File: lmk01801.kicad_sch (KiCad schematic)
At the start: 41 parts, among them J1001 142-0701-201, J1002 U.FL-R-SMT(10), J1003 U.FL-R-SMT(10), J1004 142-0701-201, J1005 U.FL-R-SMT(10), T1001 TCM2-43X+, T1002 TCM2-43X+, U1001 TCP-2-33W+, U1002 LMK01801BISQE/NOPB

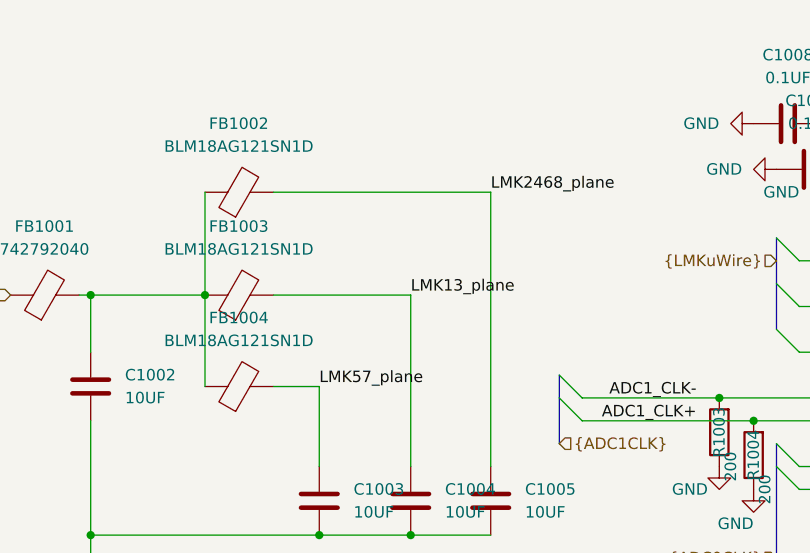
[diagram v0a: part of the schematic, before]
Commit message: Updates from Michal to fix ERC errors
Still lots of ERC warnings
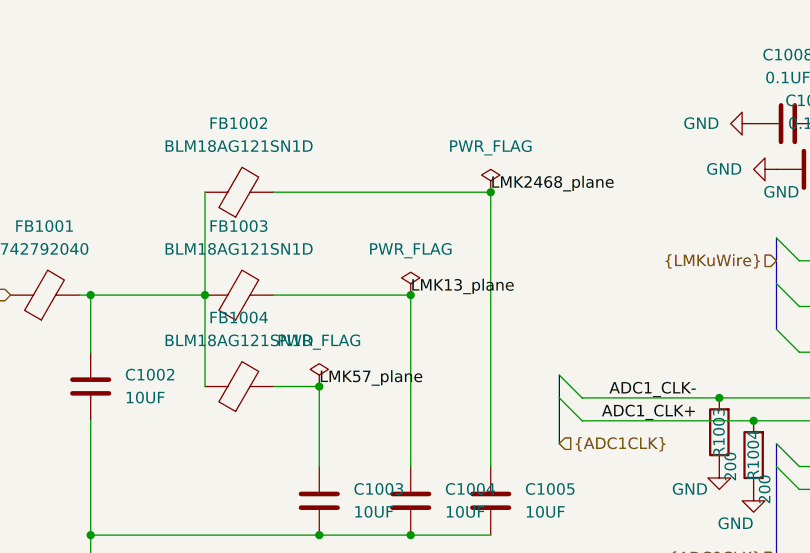
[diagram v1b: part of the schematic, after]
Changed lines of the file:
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@@
 	)
 	(junction
+		(at 64.77 54.61)
+		(diameter 0)
+		(color 0 0 0 0)
+	)
+	(junction
 		(at 123.19 114.3)
 		(diameter 0)
@@
 	)
 	(junction
+		(at 83.82 33.02)
+		(diameter 0)
+		(color 0 0 0 0)
+	)
+	(junction
 		(at 120.65 63.5)
 		(diameter 0)
@@
 		(color 0 0 0 0)
 	)
+	(junction
+		(at 74.93 44.45)
+		(diameter 0)
+		(color 0 0 0 0)
+	)
 	(no_connect
 		(at 245.11 106.68)
@@
 	(wire
 		(pts
+			(xy 120.65 25.4) (xy 143.51 25.4)
+		)
+		(stroke
+			(width 0)
+			(type default)
+		)
+	)
+	(wire
+		(pts
 			(xy 35.56 124.46) (xy 39.37 124.46)
 		)
@@
 	(wire
 		(pts
-			(xy 120.65 25.4) (xy 143.51 25.4)
-		)
-		(stroke
-			(width 0)
-			(type default)
-		)
-	)
-	(wire
-		(pts
 			(xy 245.11 33.02) (xy 266.7 33.02)
 		)
@@
 	)
 	(symbol
+		(lib_id "power:PWR_FLAG")
+		(at 64.77 54.61 0)
+		(unit 1)
+		(exclude_from_sim no)
+		(in_bom yes)
+		(on_board yes)
+		(dnp no)
+		(fields_autoplaced yes)
+		(property "Reference" "#FLG03"
+			(at 64.77 52.705 0)
+			(effects
+				(font
+					(size 1.27 1.27)
+				)
+				(hide yes)
+			)
+		)
+		(property "Value" "PWR_FLAG"
+			(at 64.77 49.53 0)
+			(effects
+				(font
+					(size 1.27 1.27)
+				)
+			)
+		)
+		(property "Footprint" ""
+			(at 64.77 54.61 0)
+			(effects
+				(font
+					(size 1.27 1.27)
+				)
+				(hide yes)
+			)
+		)
+		(property "Datasheet" "~"
+			(at 64.77 54.61 0)
+			(effects
+				(font
+					(size 1.27 1.27)
+				)
+				(hide yes)
+			)
+		)
+		(property "Description" "Special symbol for telling ERC where power comes from"
+			(at 64.77 54.61 0)
+			(effects
+				(font
+					(size 1.27 1.27)
+				)
+				(hide yes)
+			)
+		)
+		(pin "1"
+		)
+		(instances
+			(project "zest"
+				(path "/00000000-0000-0000-0000-000000000003/00000000-0000-0000-0000-000000000015"
+					(reference "#FLG03")
+					(unit 1)
+				)
+			)
+		)
+	)
+	(symbol
 		(lib_id "power:GND")
 		(at 214.63 157.48 0)
@@
 	)
 	(symbol
+		(lib_id "power:PWR_FLAG")
+		(at 83.82 33.02 0)
+		(unit 1)
+		(exclude_from_sim no)
+		(in_bom yes)
+		(on_board yes)
+		(dnp no)
+		(fields_autoplaced yes)
+		(property "Reference" "#FLG01"
+			(at 83.82 31.115 0)
+			(effects
+				(font
+					(size 1.27 1.27)
+				)
+				(hide yes)
+			)
+		)
+		(property "Value" "PWR_FLAG"
+			(at 83.82 27.94 0)
+			(effects
+				(font
+					(size 1.27 1.27)
+				)
+			)
+		)
+		(property "Footprint" ""
+			(at 83.82 33.02 0)
+			(effects
+				(font
+					(size 1.27 1.27)
+				)
+				(hide yes)
+			)
+		)
+		(property "Datasheet" "~"
+			(at 83.82 33.02 0)
+			(effects
+				(font
+					(size 1.27 1.27)
+				)
+				(hide yes)
+			)
+		)
+		(property "Description" "Special symbol for telling ERC where power comes from"
+			(at 83.82 33.02 0)
+			(effects
+				(font
+					(size 1.27 1.27)
+				)
+				(hide yes)
+			)
+		)
+		(pin "1"
+		)
+		(instances
+			(project "zest"
+				(path "/00000000-0000-0000-0000-000000000003/00000000-0000-0000-0000-000000000015"
+					(reference "#FLG01")
+					(unit 1)
+				)
+			)
+		)
+	)
+	(symbol
 		(lib_id "Device:C")
 		(at 264.16 25.4 90)
@@
 					(unit 1)
 				)
+			)
+		)
+	)
+	(symbol
+		(lib_id "power:PWR_FLAG")
+		(at 74.93 44.45 0)
+		(unit 1)
+		(exclude_from_sim no)
+		(in_bom yes)
+		(on_board yes)
+		(dnp no)
+		(fields_autoplaced yes)
+		(property "Reference" "#FLG02"
+			(at 74.93 42.545 0)
+			(effects
+				(font
+					(size 1.27 1.27)
+				)
+				(hide yes)
+			)
+		)
+		(property "Value" "PWR_FLAG"
+			(at 74.93 39.37 0)
+			(effects
+				(font
+					(size 1.27 1.27)
+				)
+			)
+		)
+		(property "Footprint" ""
+			(at 74.93 44.45 0)
+			(effects
+				(font
+					(size 1.27 1.27)
+				)
+				(hide yes)
+			)
+		)
+		(property "Datasheet" "~"
+			(at 74.93 44.45 0)
+			(effects
+				(font
+					(size 1.27 1.27)
+				)
+				(hide yes)
+			)
+		)
+		(property "Description" "Special symbol for telling ERC where power comes from"
+			(at 74.93 44.45 0)
+			(effects
+				(font
+					(size 1.27 1.27)
+				)
+				(hide yes)
+			)
+		)
+		(pin "1"
+		)
+		(instances
+			(project "zest"
+				(path "/00000000-0000-0000-0000-000000000003/00000000-0000-0000-0000-000000000015"
+					(reference "#FLG02")
+					(unit 1)
+				)

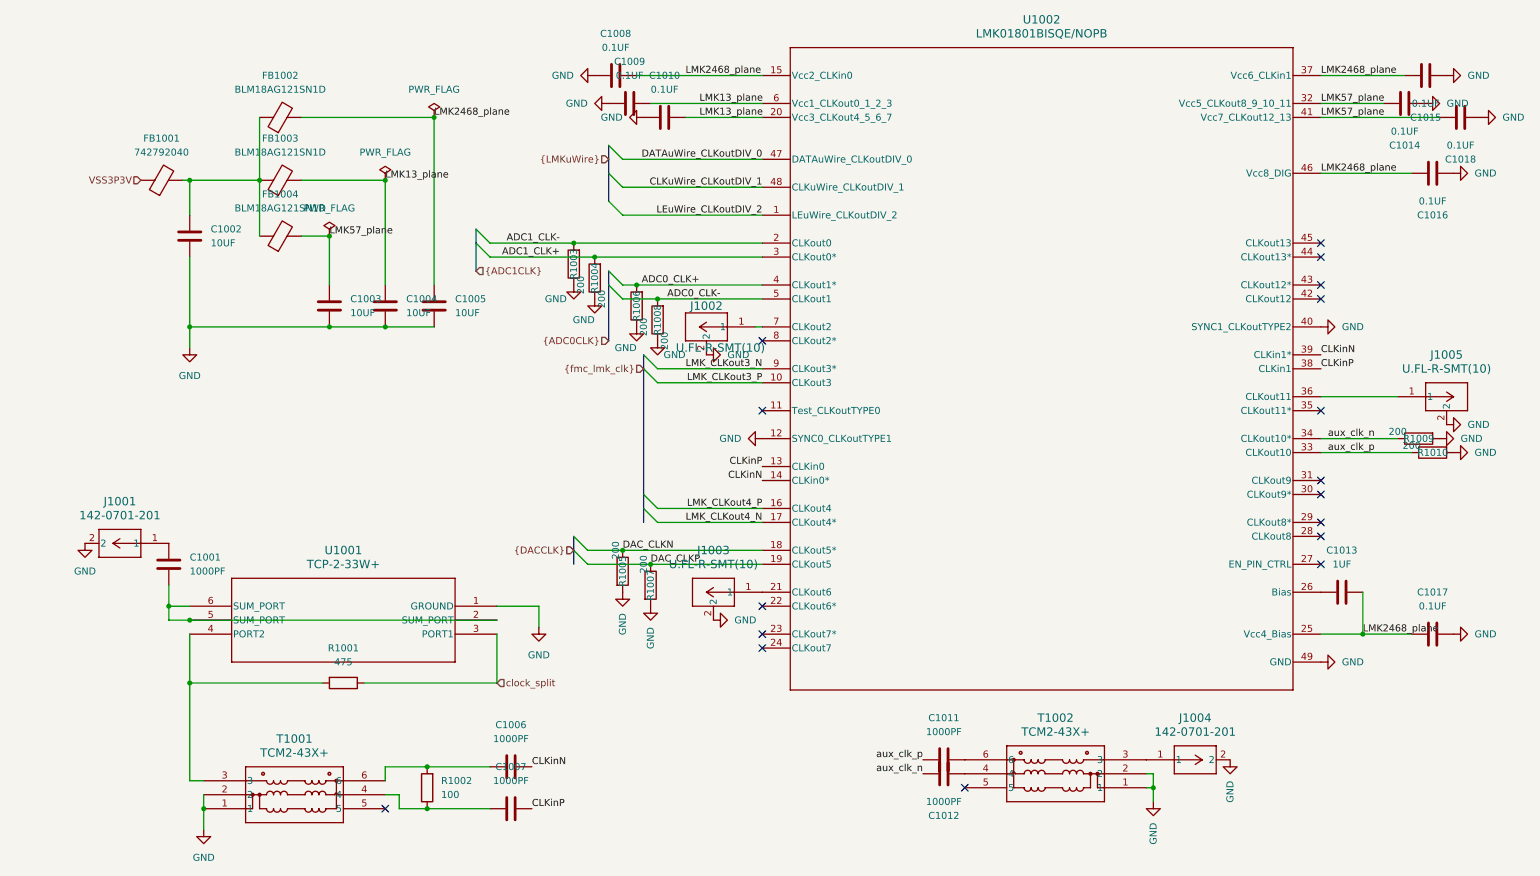
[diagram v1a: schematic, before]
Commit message: Schematic Changes
Added Manufacturer/MPN/Description Fields to parts
Added libraries to project
Modified FMC schematic to use new symbol
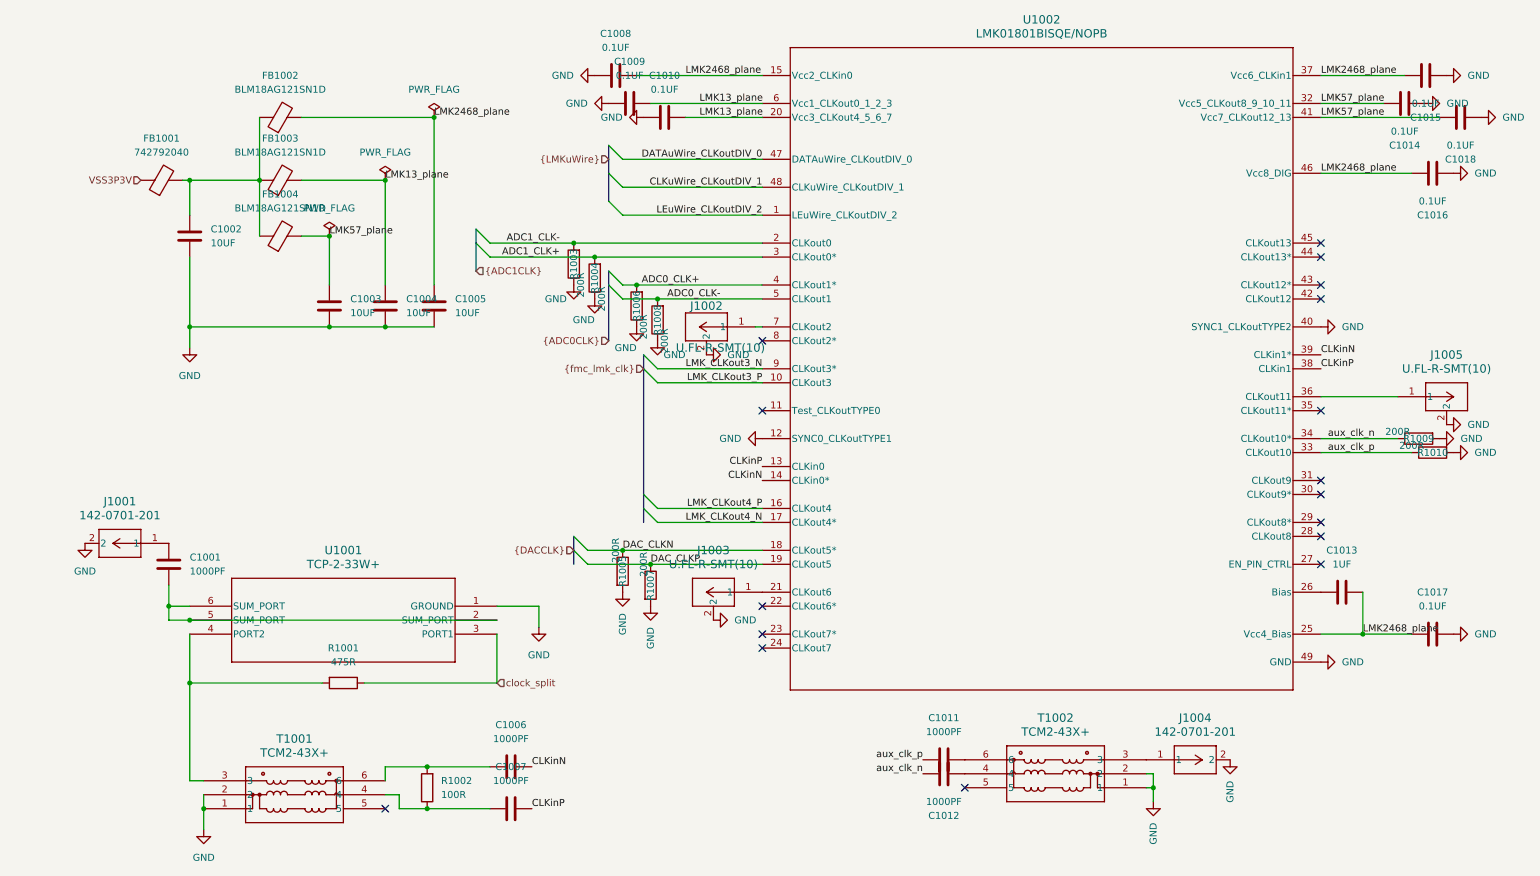
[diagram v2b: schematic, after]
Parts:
- C1001, C1006, C1007, C1011, C1012: Manufacturer (none) -> Murata; Manufacturer Part Number (none) -> GRM1885C1H102JA01D
- C1002, C1003, C1004, C1005: Manufacturer (none) -> TDK; Manufacturer Part Number (none) -> C1608X5R1A106M080AC
- C1008, C1009, C1010, C1014, C1015, C1016, C1017, C1018: Manufacturer (none) -> Murata; Manufacturer Part Number (none) -> GRM155R61A104KA01D
- C1013: Manufacturer (none) -> Murata; Manufacturer Part Number (none) -> GRM188R61E105KA12D
- FB1001: Manufacturer (none) -> Würth; Manufacturer Part Number (none) -> 742792040
- FB1002, FB1003, FB1004: Manufacturer (none) -> Murata; Manufacturer Part Number (none) -> BLM18AG121SN1D
- J1001, J1004: Manufacturer (none) -> Cinch; Manufacturer Part Number (none) -> 142-0701-201
- J1002, J1003, J1005: Manufacturer (none) -> Hirose; Manufacturer Part Number (none) -> U.FL-R-SMT(10)
- R1001: value 475 -> 475R; Manufacturer (none) -> YAGEO; Manufacturer Part Number (none) -> RC0603FR-07475RL
- R1002: value 100 -> 100R; Manufacturer (none) -> YAGEO; Manufacturer Part Number (none) -> RC0603FR-07100RL
- R1003, R1004, R1005, R1006, R1007, R1008, R1009, R1010: value 200 -> 200R; Manufacturer (none) -> Susumu; Manufacturer Part Number (none) -> RR0816P-201-D
- T1001, T1002: Manufacturer (none) -> Mini-Circuits; Manufacturer Part Number (none) -> TCM2-43X+
- U1001: Manufacturer (none) -> Mini-Circuits; Manufacturer Part Number (none) -> TCP-2-33W+
- U1002: Manufacturer (none) -> Texas Instruments; Manufacturer Part Number (none) -> LMK01801BISQE/NOPB

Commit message: Schematics update
Cleaned up RF ADC and front end sections.
Verified that changes did not changes anything about the layout.
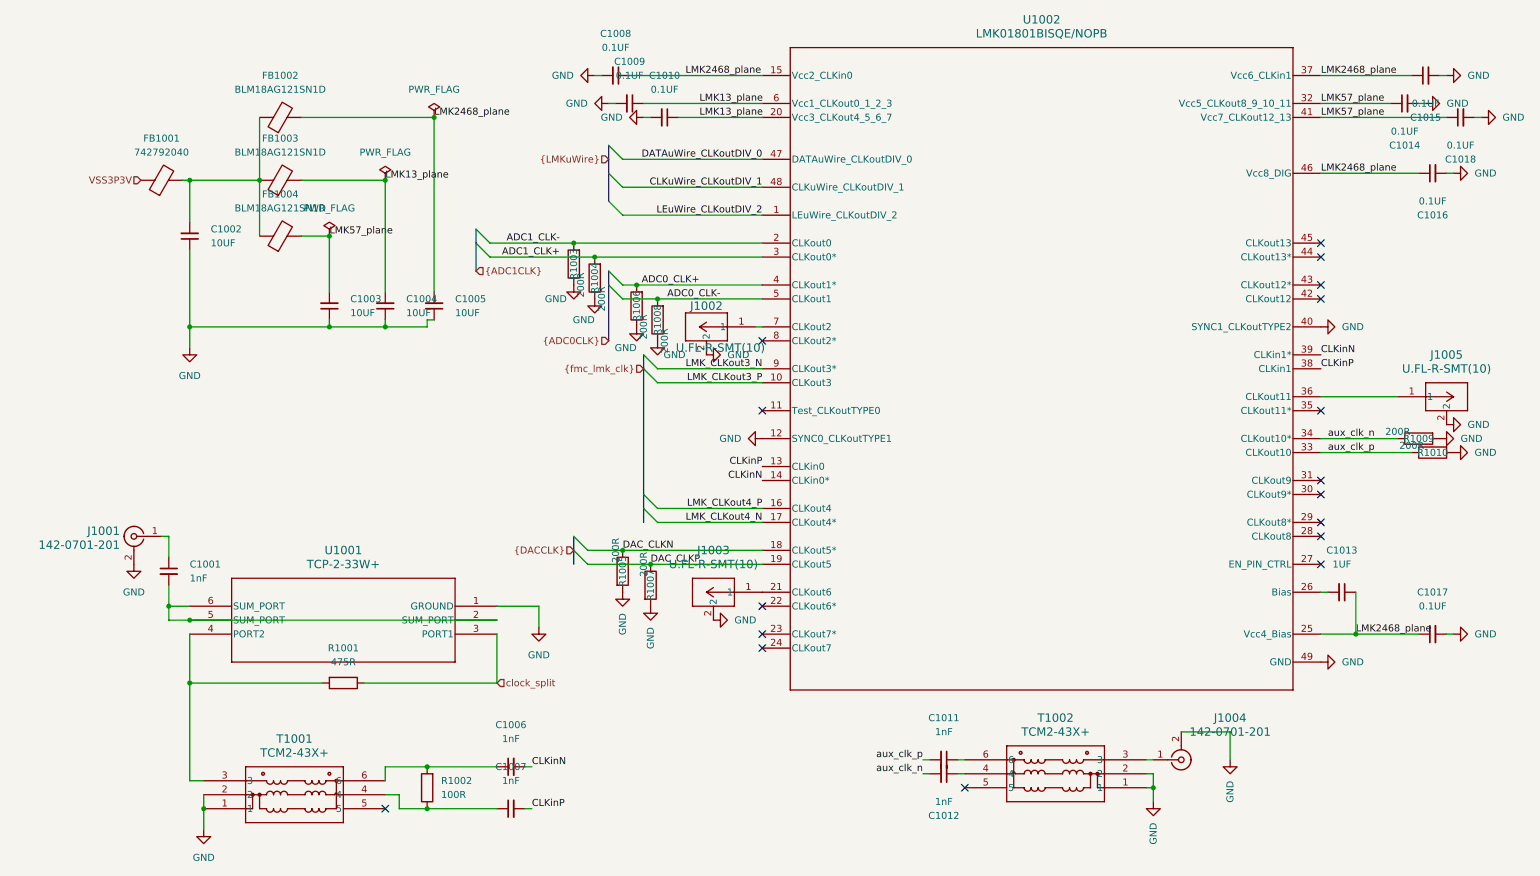
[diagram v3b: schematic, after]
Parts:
- C1001, C1006, C1007, C1011, C1012: value 1000PF -> 1nF; symbol Device:C -> Device:C_Small
- C1002, C1003, C1004, C1005, C1008, C1009, C1010, C1013, C1014, C1015, C1016, C1017, C1018: symbol Device:C -> Device:C_Small
- J1001, J1004: symbol 001_symbol:142-0701-201_GH -> Zest_Custom:SMA_Coaxial
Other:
- moved on the sheet: C1001

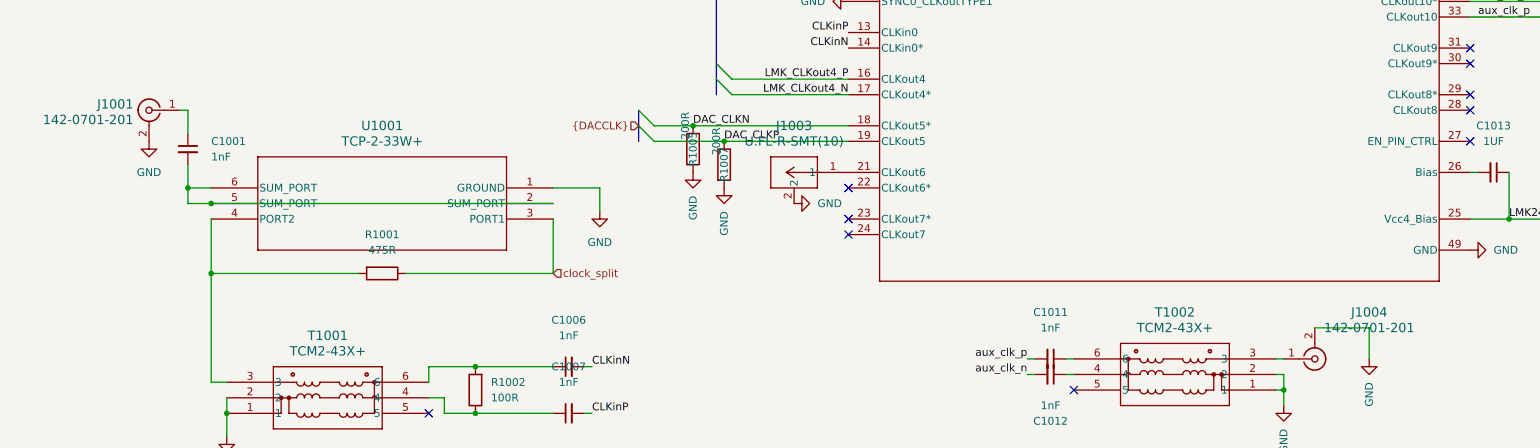
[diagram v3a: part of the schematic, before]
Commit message: Further Project cleanup
-Added BOM and fabrication files
-updated all documentation files
- Added suggested DC blocking cap at DAC outputs

-Set DRC to 5mil trace and space and fixed various violations detailed below
- Removed various small tracks overlapping IC pads on U2701,U2901,U3101,U3201
- Spaced vias 5 mil apart around U701, U201, 1201
- Moved LMK_CLKout3 pair on In4 layer away from PMOD1_1 pin
- adjusted track into pin47 on U701 to clear pin 48
- adjusted trace under U903 to give more room from ground pads/vias
- spaced out vias around pins45/46 of U201

-Many tweak to trace to go through the center of pad throughout the design
-An example is the trace around C3005
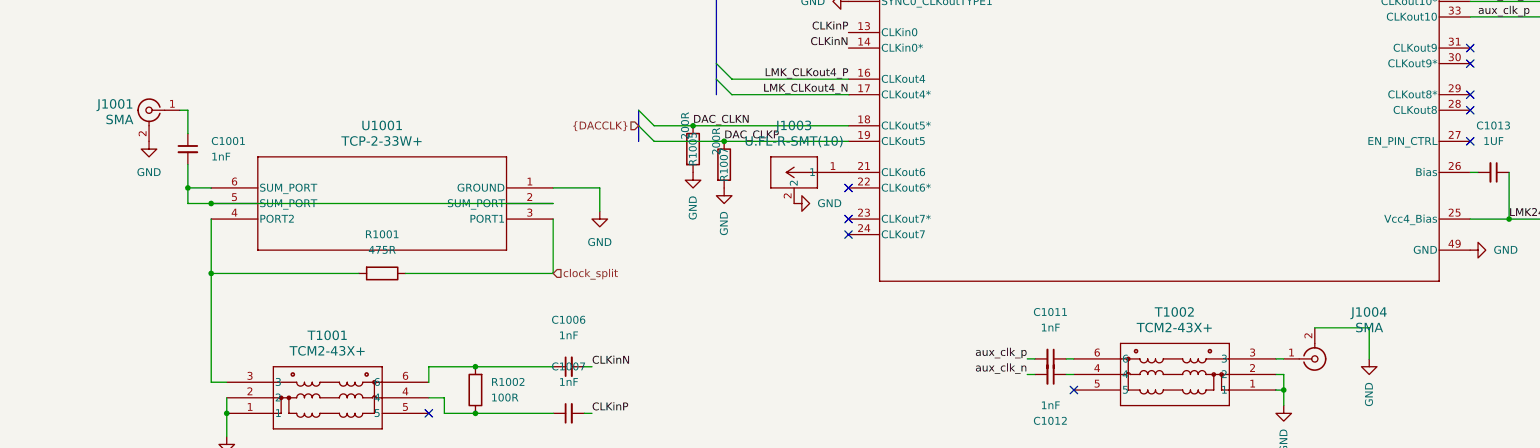
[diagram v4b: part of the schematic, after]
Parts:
- J1001, J1004: value 142-0701-201 -> SMA
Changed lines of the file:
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@@
 			)
 		)
-		(property "Value" "142-0701-201"
+		(property "Value" "SMA"
 			(at 228.6 144.78 0)
 			(effects
@@
 			)
 		)
-		(property "Value" "142-0701-201"
+		(property "Value" "SMA"
 			(at 26.67 110.7831 0)
 			(effects
